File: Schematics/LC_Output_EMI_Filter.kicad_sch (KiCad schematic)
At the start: 0 parts

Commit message: Added LCL filter to output EMI Filter
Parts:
- added C53: C, symbol Device:C
- added L3, L4: L, symbol Device:L
- added R34: R, symbol Device:R
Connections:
- new net Phase_A: L3.1
- new net Phase_A_Filtered: C53.1, L3.2, R34.1
- new net Phase_B: L4.1
- new net Phase_B_Filtered: C53.2, L4.2, R34.2
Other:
- note added: "1. A floating 120 Vrms line‑to‑line output is a valid 120 V AC source Most people think "120 V" means "120 V from hot to neutral," but electrically: • Appliances only care about the voltage across their two input terminals. • They do not require one of those terminals to be neutral or earth‑referenced. • They do not require a grounded conductor to function. A floating 2‑wire AC source is complete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"
- note added: "Line-to-Line"
- note added: "Per phase (for the full‑bridge output): - L1: 1.0 mH, ≥10 A RMS, low loss - L2: 1.0 mH, ≥10 A RMS, low loss - C: 3.3 µF, ≥250 Vac film - R_d: 8.2 Ω in series with C, a few watts"

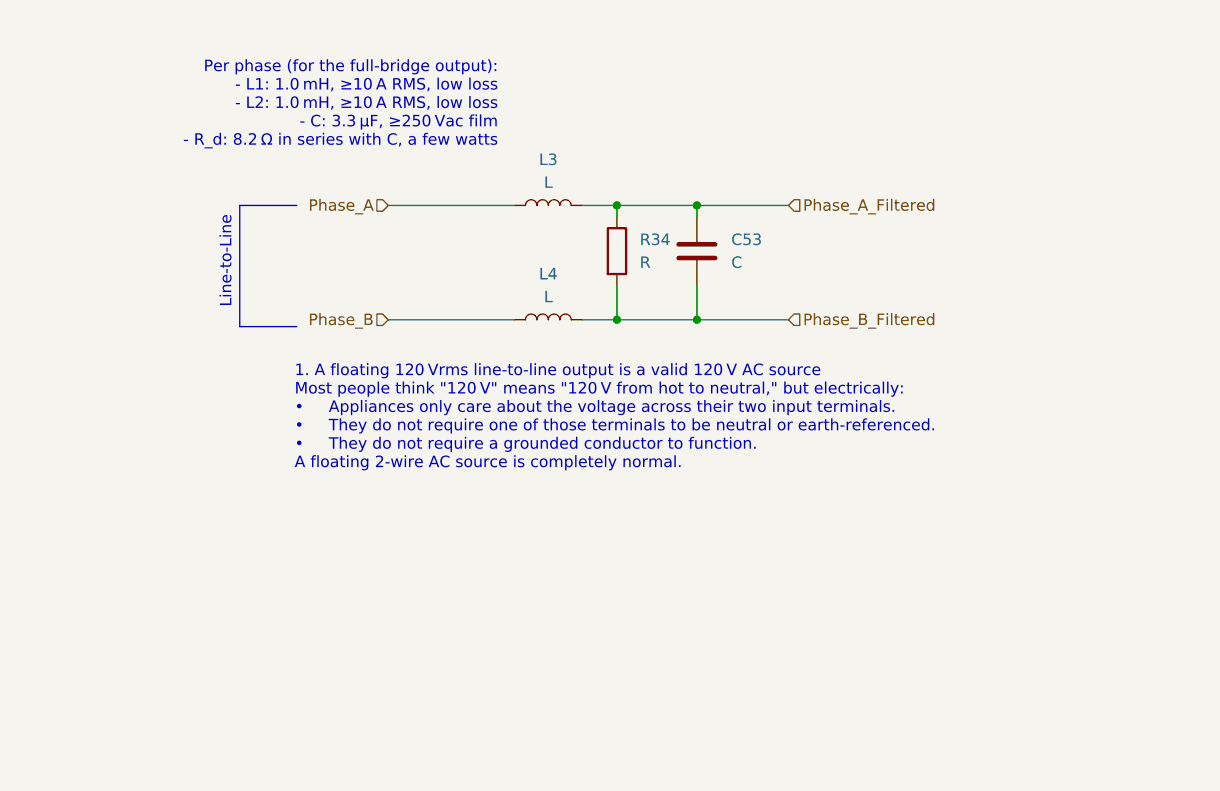
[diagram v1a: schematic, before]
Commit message: [WIP SiC Single Phase Inverter
- Updated README.md
- Added New Parts for Output filter L,C,R
- Added datasheets for the new parts
- Added 3D models for the new parts
- Added new symbols and footprints for the L,C,R
- Finished output filter
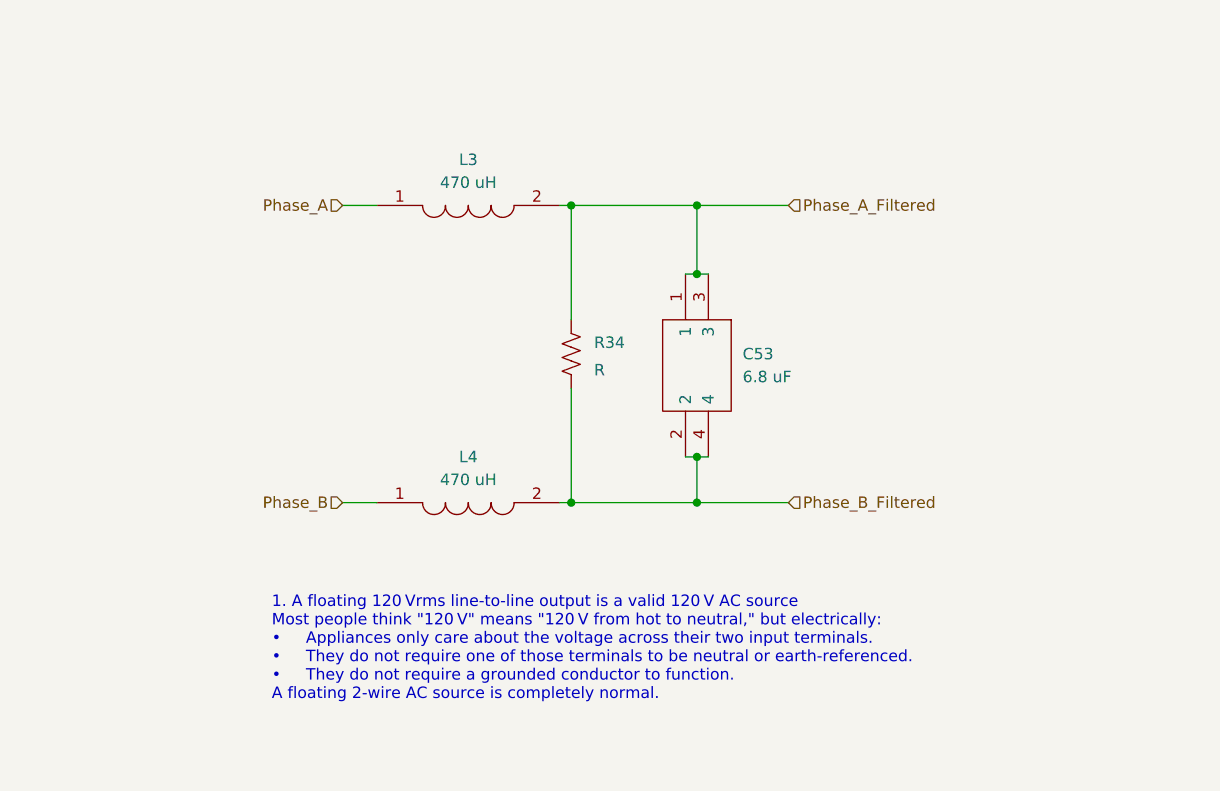
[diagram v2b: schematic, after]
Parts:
- C53: value C -> 6.8 uF; footprint (none) -> SiC_Inverter:C4AF9BW4680T3FK; symbol Device:C -> SiC_Inverter:C4AF9BW4680T3FK; Height (none) -> 40.2; Manufacturer_Name (none) -> Yageo Group; Manufacturer_Part_Number (none) -> C4AF9BW4680T3FK
- L3, L4: value L -> 470 uH; footprint (none) -> SiC_Inverter:1140471KRC; symbol Device:L -> SiC_Inverter:1140-471K-RC; Height (none) -> 26.162; Manufacturer_Name (none) -> Bourns; Manufacturer_Part_Number (none) -> 1140-471K-RC; Mouser Part Number (none) -> 542-1140-471K-RC; Mouser Price/Stock (none) -> https://www.mouser.co.uk/ProductDetail/Bourns/1140-471K-RC?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
- R34: footprint (none) -> SiC_Inverter:CW005100R0JE12HE; symbol Device:R -> SiC_Inverter:3-2176794-3
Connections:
- net Phase_A_Filtered: now also C53.3
- net Phase_B_Filtered: now also C53.4
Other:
- note removed: "Line-to-Line"
- note removed: "Per phase (for the full‑bridge output): - L1: 1.0 mH, ≥10 A RMS, low loss - L2: 1.0 mH, ≥10 A RMS, low loss - C: 3.3 µF, ≥250 Vac film - R_d: 8.2 Ω in series with C, a few watts"

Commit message: Changing Text to Text Block
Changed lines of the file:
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@@
 	(generator_version "9.0")
 	(paper "A4")
+	(rectangle
+		(start 103.886 83.566)
+		(end 185.166 126.492)
+		(stroke
+			(width 0)
+			(type default)
+		)
+		(fill
+			(type none)
+		)
+	)
 	(text "1. A floating 120 Vrms line‑to‑line output is a valid 120 V AC source\nMost people think \"120 V\" means \"120 V from hot to neutral,\" but electrically:\n• 	Appliances only care about the voltage across their two input terminals.\n• 	They do not require one of those terminals to be neutral or earth‑referenced.\n• 	They do not require a grounded conductor to function.\nA floating 2‑wire AC source is completely normal.\n"
 		(exclude_from_sim no)
-		(at 108.966 136.906 0)
+		(at 103.886 133.604 0)
 		(effects
 			(font
@@
 		)
 	)
+	(text_box "LCL AC Output Filter"
+		(exclude_from_sim no)
+		(at 103.886 80.01 0)
+		(size 23.622 3.048)
+		(margins 0.9525 0.9525 0.9525 0.9525)
+		(stroke
+			(width 0)
+			(type solid)
+		)
+		(fill
+			(type color)
+			(color 0 0 255 0.1)
+		)
+		(effects
+			(font
+				(size 1.27 1.27)
+			)
+			(justify left top)
+		)
+	)

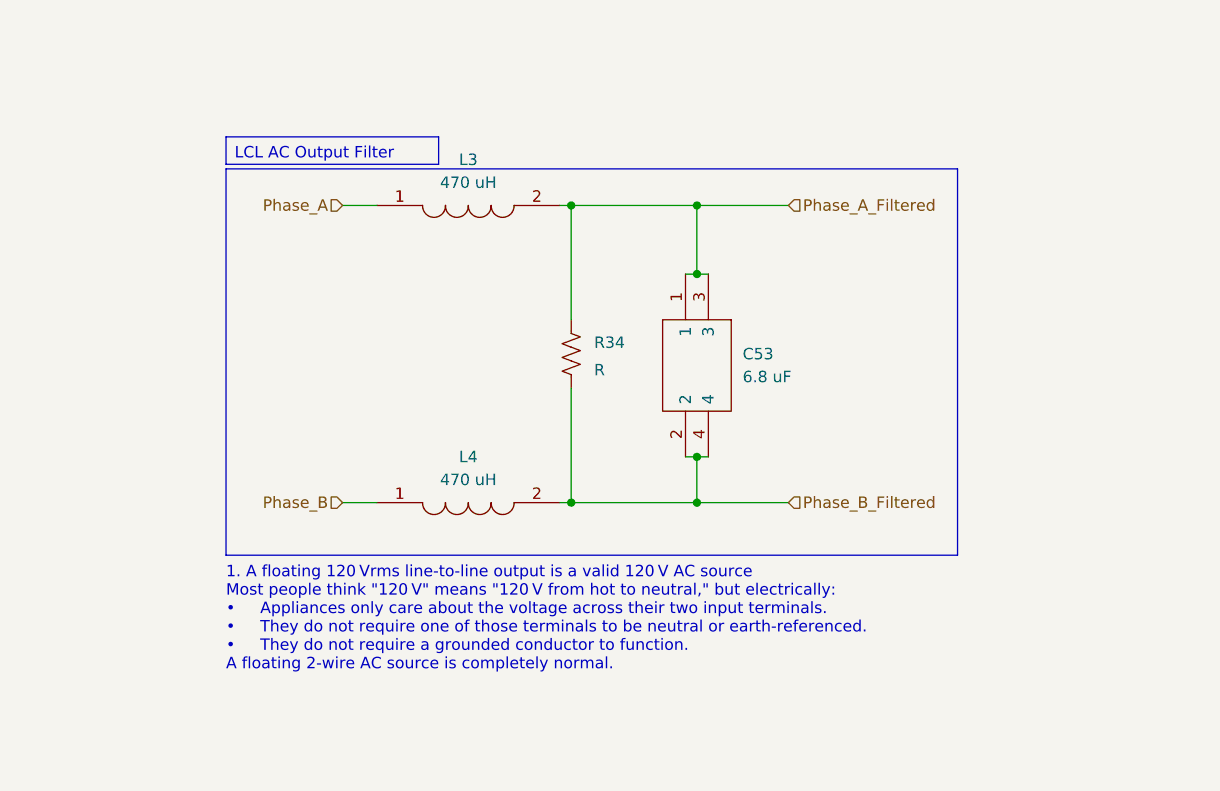
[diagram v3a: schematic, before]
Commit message: [WIP Single Phase SiC Inverter]
- Added molex 4 pin pcb connector for +15V power
- Added 3d model, symbol and footprint
- Added datasheet for molex connector
- Added Male and Female pcb - pcb connectors to all sub sheets
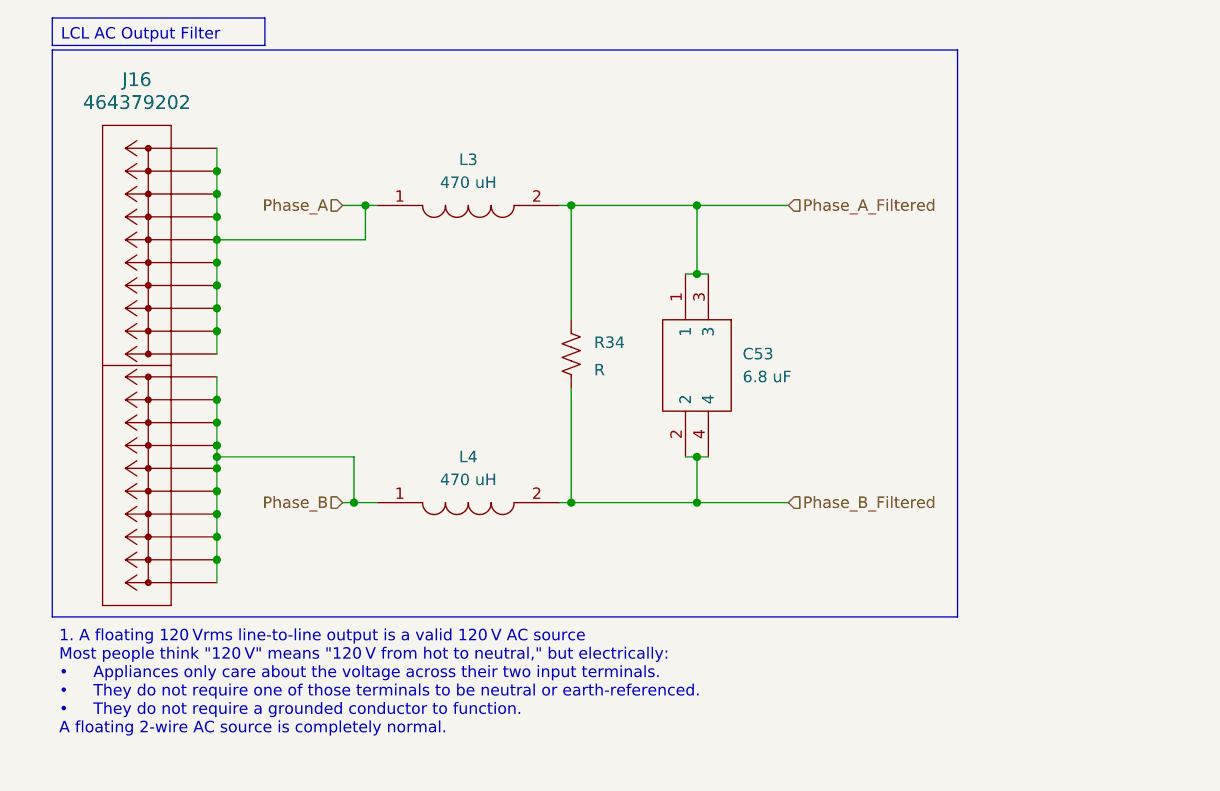
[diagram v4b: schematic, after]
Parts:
- added J16: 464379202, SiC_Inverter:46437-900_02, symbol SiC_Inverter:464379202
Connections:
- net Phase_A: now also J16.P2_1, J16.P2_10, J16.P2_2, J16.P2_3, J16.P2_4, J16.P2_5, J16.P2_6, J16.P2_7, J16.P2_8, J16.P2_9
- net Phase_B: now also J16.P1_1, J16.P1_10, J16.P1_2, J16.P1_3, J16.P1_4, J16.P1_5, J16.P1_6, J16.P1_7, J16.P1_8, J16.P1_9

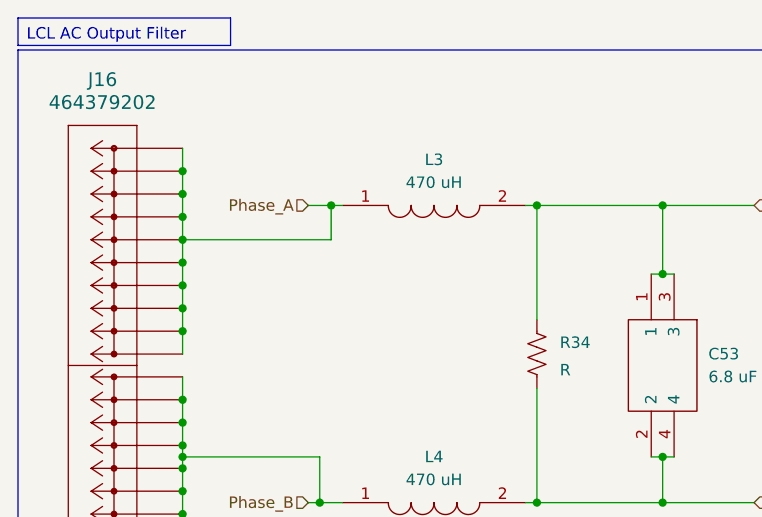
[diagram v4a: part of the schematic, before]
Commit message: [WIP Single Phase Inverter]
- Changed all Refs within each sub sheet (Stripe)
- Added 3V3 Power Supply off of 15V iso supply
- Added footprint, symbol and 3d part
- updated PCB with new part
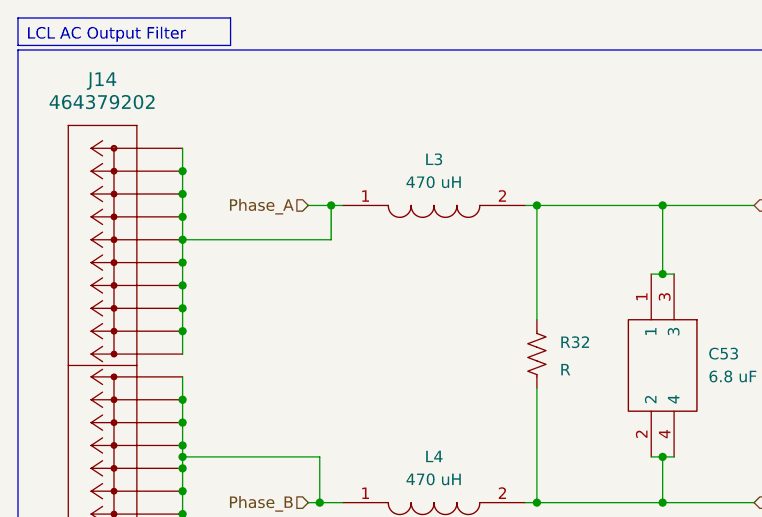
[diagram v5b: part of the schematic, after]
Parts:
- renumbered J16 to J14, R34 to R32
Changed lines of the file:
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@@
 		(on_board yes)
 		(dnp no)
-		(property "Reference" "R34"
+		(property "Reference" "R32"
 			(at 144.78 102.8699 0)
 			(effects
@@
 			(project ""
 				(path "/a1ed0539-9735-4ad1-a8fd-87e26e7fce16/bc0f80e1-b57d-46ec-8488-4a939507ae45"
-					(reference "R34")
+					(reference "R32")
 					(unit 1)
 				)
@@
 		(dnp no)
 		(fields_autoplaced yes)
-		(property "Reference" "J16"
+		(property "Reference" "J14"
 			(at 93.98 73.66 0)
 			(effects
@@
 			(project "SiC_Single_Phase_Inverter"
 				(path "/a1ed0539-9735-4ad1-a8fd-87e26e7fce16/bc0f80e1-b57d-46ec-8488-4a939507ae45"
-					(reference "J16")
-					(unit 1)
-				)
+					(reference "J14")
+					(unit 1)
+				)

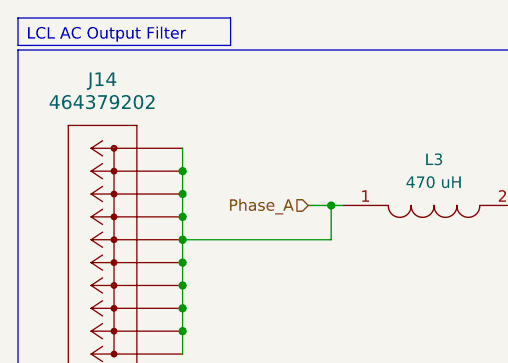
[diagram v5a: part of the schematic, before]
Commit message: [Milestone Compelted Controller and USB]
- Added Test Points
- Completed USB circuit to Controller
- Wired up Controller
- Added Connectors to Power Subsheet and 12pin from cotnroller to Full
  Bridge
- Added 3d models for USB compoents
- General fixes to subsheets
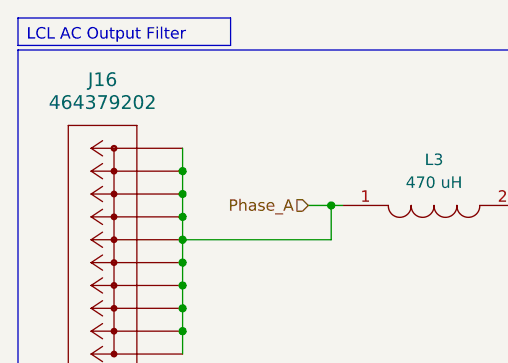
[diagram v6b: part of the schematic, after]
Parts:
- renumbered J14 to J16
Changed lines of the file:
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@@
 		(dnp no)
 		(fields_autoplaced yes)
-		(property "Reference" "J14"
+		(property "Reference" "J16"
 			(at 93.98 73.66 0)
 			(effects
@@
 			(project "SiC_Single_Phase_Inverter"
 				(path "/a1ed0539-9735-4ad1-a8fd-87e26e7fce16/bc0f80e1-b57d-46ec-8488-4a939507ae45"
-					(reference "J14")
+					(reference "J16")
 					(unit 1)
 				)

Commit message: WIP PCB, Added Test Points, added icon file
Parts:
- renumbered J16 to J17, R32 to R33
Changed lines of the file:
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@@
 		(on_board yes)
 		(dnp no)
-		(property "Reference" "R32"
+		(property "Reference" "R33"
 			(at 144.78 102.8699 0)
 			(effects
@@
 			(project ""
 				(path "/a1ed0539-9735-4ad1-a8fd-87e26e7fce16/bc0f80e1-b57d-46ec-8488-4a939507ae45"
-					(reference "R32")
+					(reference "R33")
 					(unit 1)
 				)
@@
 		(dnp no)
 		(fields_autoplaced yes)
-		(property "Reference" "J16"
+		(property "Reference" "J17"
 			(at 93.98 73.66 0)
 			(effects
@@
 			(project "SiC_Single_Phase_Inverter"
 				(path "/a1ed0539-9735-4ad1-a8fd-87e26e7fce16/bc0f80e1-b57d-46ec-8488-4a939507ae45"
-					(reference "J16")
-					(unit 1)
-				)
+					(reference "J17")
+					(unit 1)
+				)

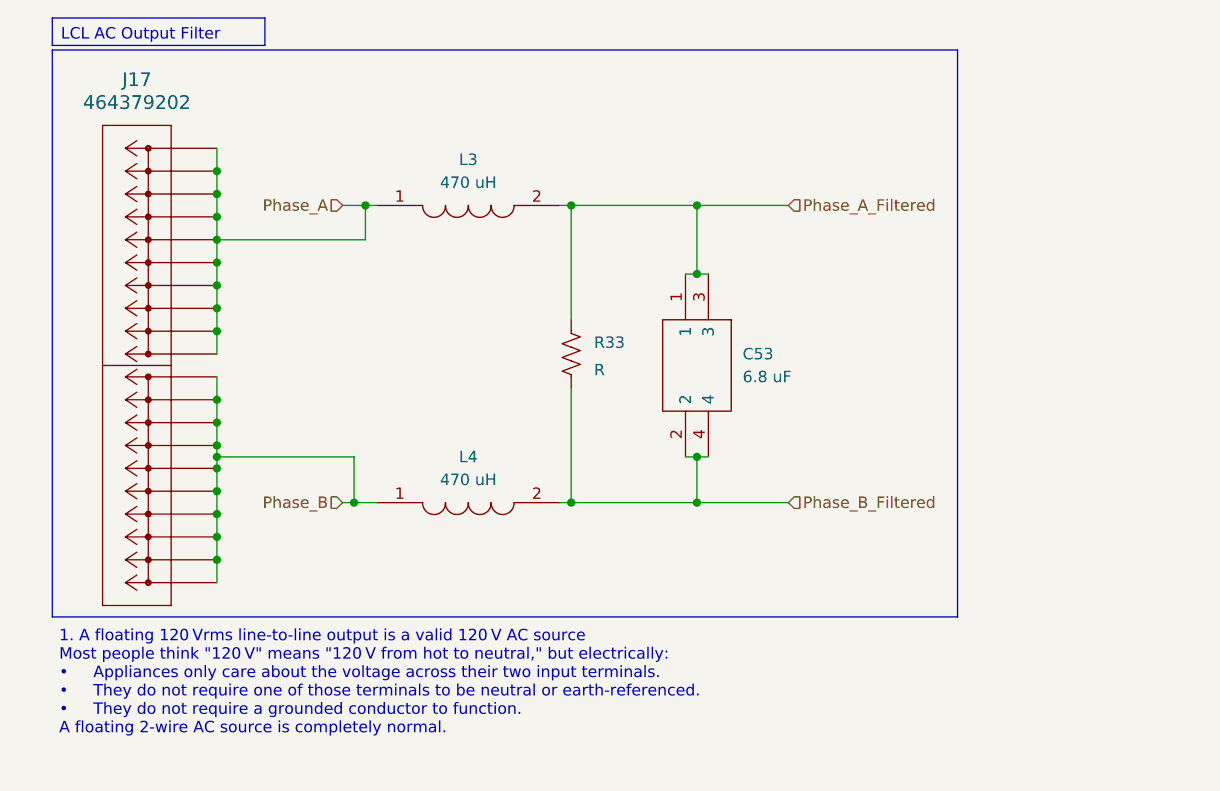
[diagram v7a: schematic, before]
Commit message: WIP PCB Design: Finished DC Input / Protection Circuit
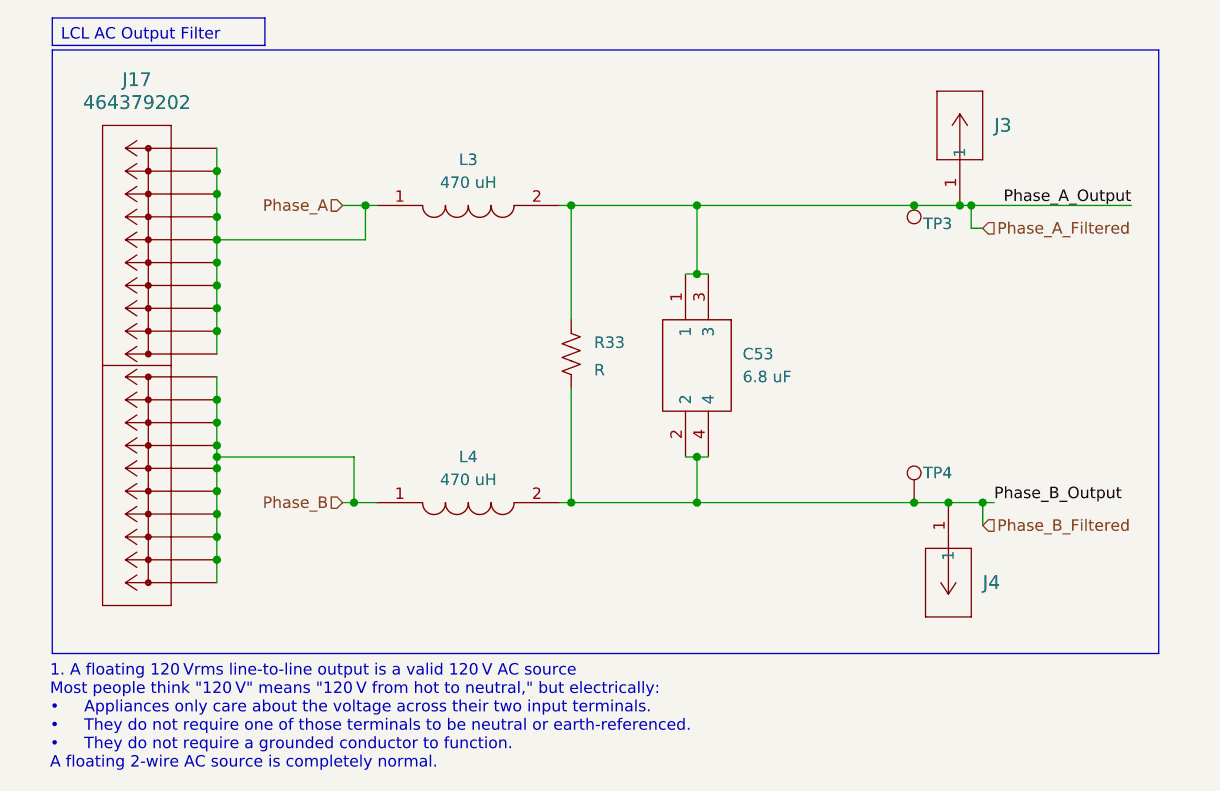
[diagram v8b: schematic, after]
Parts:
- added J3: 23AH8786-Red, SiC_Inverter:23AH8786-Red, symbol SiC_Inverter:23AH8786-Red
- added J4: 23AH8785-Black, SiC_Inverter:23AH8785-Black, symbol SiC_Inverter:23AH8785-Black
- added TP3: 5277, SiC_Inverter:5277, symbol SiC_Inverter:5277
- added TP4: 5281, SiC_Inverter:5281, symbol SiC_Inverter:5281
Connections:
- net Phase_A_Filtered: now also J3.1, TP3.1
- net Phase_B_Filtered: now also J4.1, TP4.1
